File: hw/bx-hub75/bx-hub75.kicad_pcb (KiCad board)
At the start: 2 copper layers, 63.5 x 50.8 mm, 11 parts, among them J1 DB9_Male, U1 74HCT244, U2 74HCT244, U3 LD1117S33TR_SOT223, U4 25LCxxx, U5 SN65HVD77D

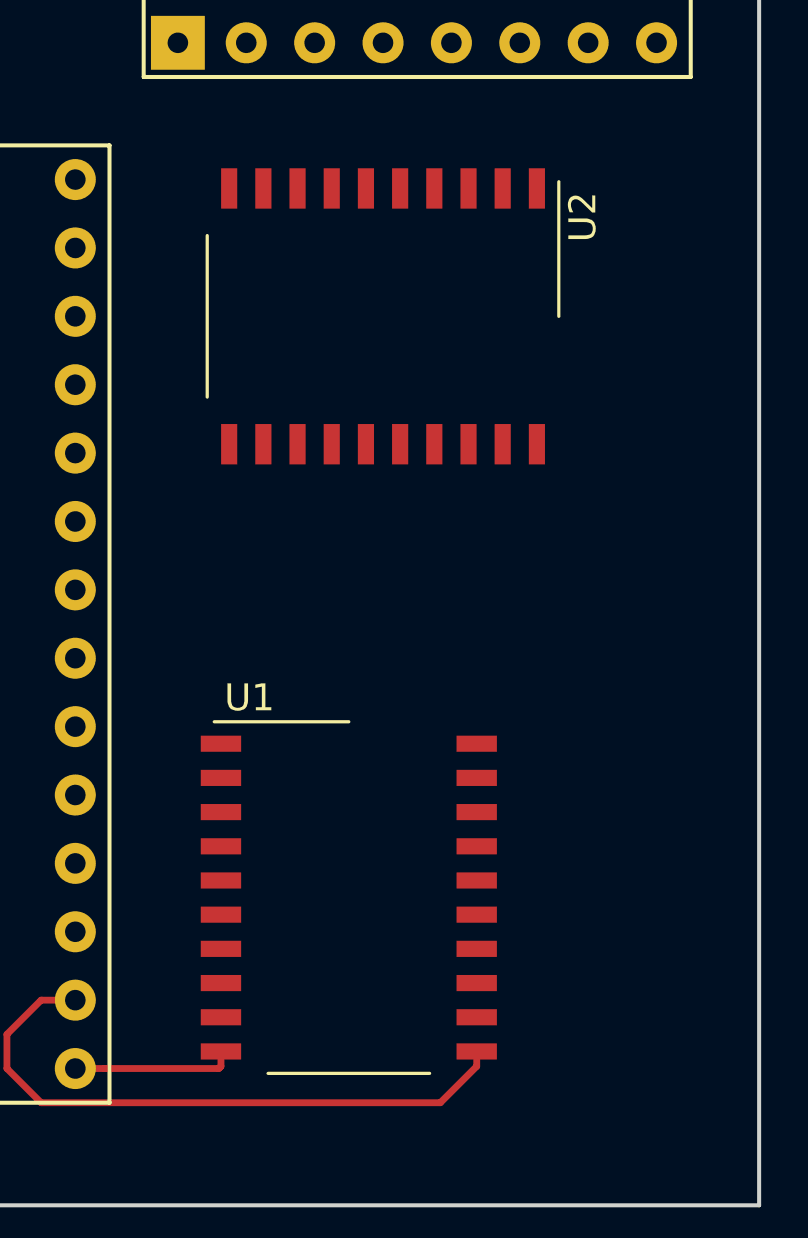
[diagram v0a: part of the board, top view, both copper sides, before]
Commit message: hw/bx-hub75: 74HCT244 -> 74HCT541
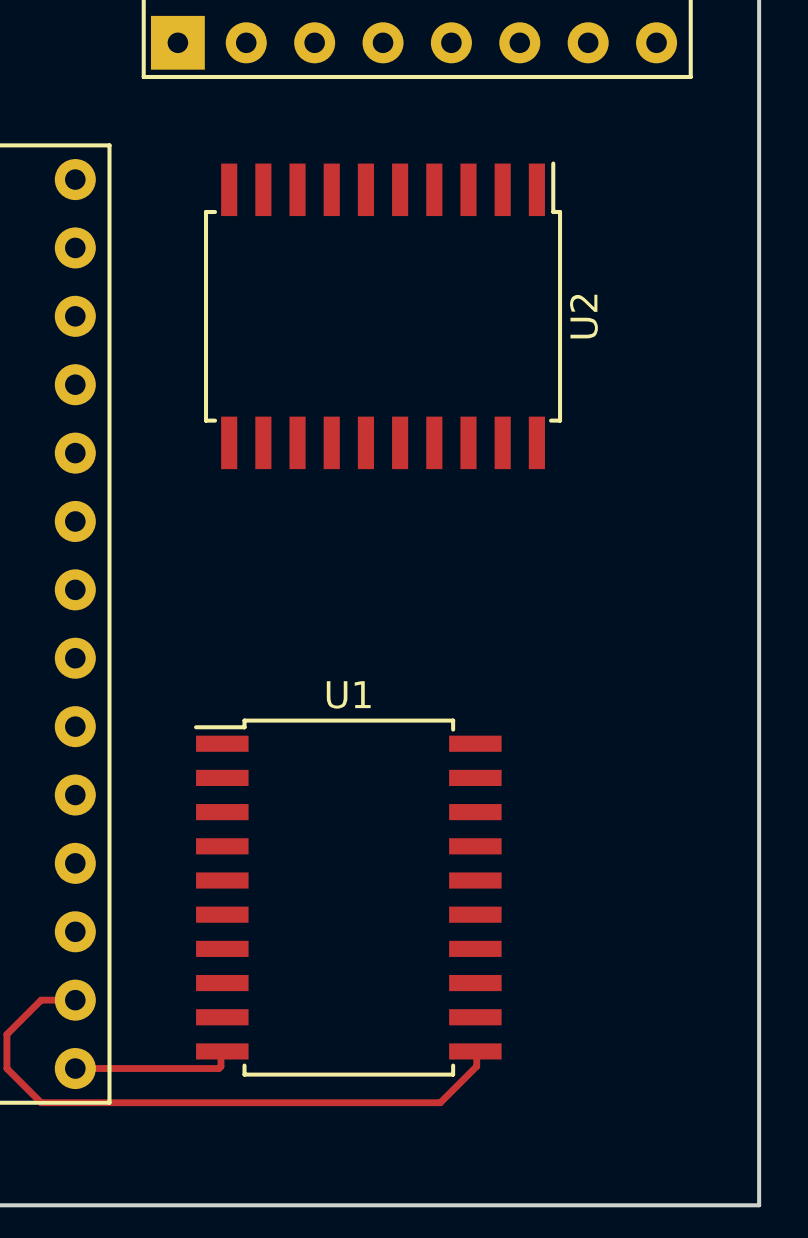
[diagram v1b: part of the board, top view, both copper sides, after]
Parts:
- U1, U2: value 74HCT244 -> 74HCT541; footprint Package_SO:SO-20_12.8x7.5mm_P1.27mm -> Package_SO:SOIC-20W_7.5x12.8mm_P1.27mm
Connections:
- U1 pad 11: /OE -> Net-(CHAIN1-Pad15)
- U1 pad 12: Net-(CHAIN1-Pad7) -> Net-(CHAIN1-Pad13)
- U1 pad 13: /CLK -> Net-(CHAIN1-Pad11)
- U1 pad 14: Net-(CHAIN1-Pad5) -> Net-(CHAIN1-Pad9)
- U1 pad 15: /C -> Net-(CHAIN1-Pad7)
- U1 pad 16: Net-(CHAIN1-Pad3) -> Net-(CHAIN1-Pad5)
- U1 pad 17: /A -> Net-(CHAIN1-Pad3)
- U1 pad 3: Net-(CHAIN1-Pad9) -> /B1
- U1 pad 4: /B1 -> /R2
- U1 pad 5: Net-(CHAIN1-Pad11) -> /B2
- U1 pad 6: /R2 -> /A
- U1 pad 7: Net-(CHAIN1-Pad13) -> /C
- U1 pad 8: /B2 -> /CLK
- U1 pad 9: Net-(CHAIN1-Pad15) -> /OE
- U2 pad 12: Net-(CHAIN1-Pad6) -> Net-(U2-Pad12)
- U2 pad 14: Net-(CHAIN1-Pad10) -> Net-(CHAIN1-Pad2)
- U2 pad 15: Net-(U2-Pad15) -> Net-(CHAIN1-Pad6)
- U2 pad 16: Net-(CHAIN1-Pad12) -> Net-(CHAIN1-Pad10)
- U2 pad 17: /G1 -> Net-(CHAIN1-Pad12)
- U2 pad 3: Net-(CHAIN1-Pad2) -> /D
- U2 pad 4: /D -> /B
- U2 pad 5: Net-(U2-Pad5) -> /G2
- U2 pad 6: /B -> /G1
- U2 pad 8: /G2 -> Net-(U2-Pad8)

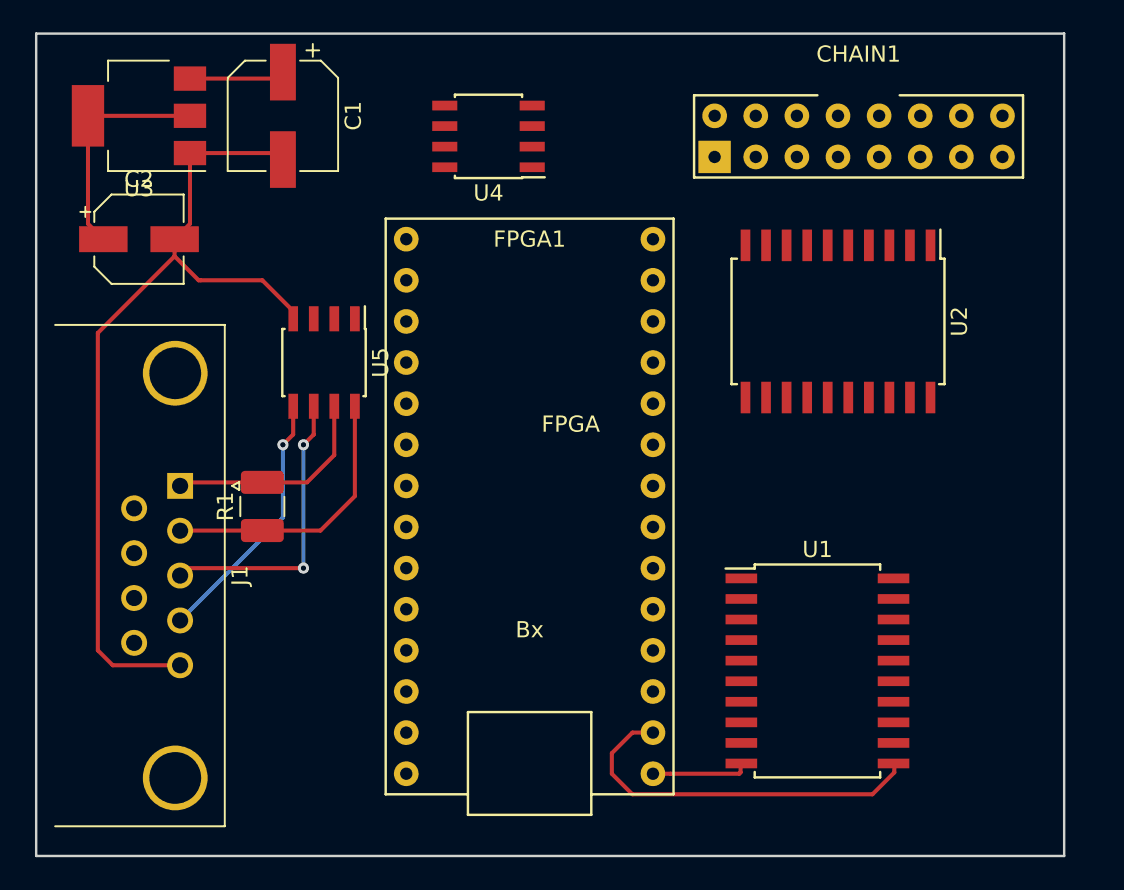
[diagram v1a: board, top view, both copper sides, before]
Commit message: hw/bx-hub75: finish basic routing.
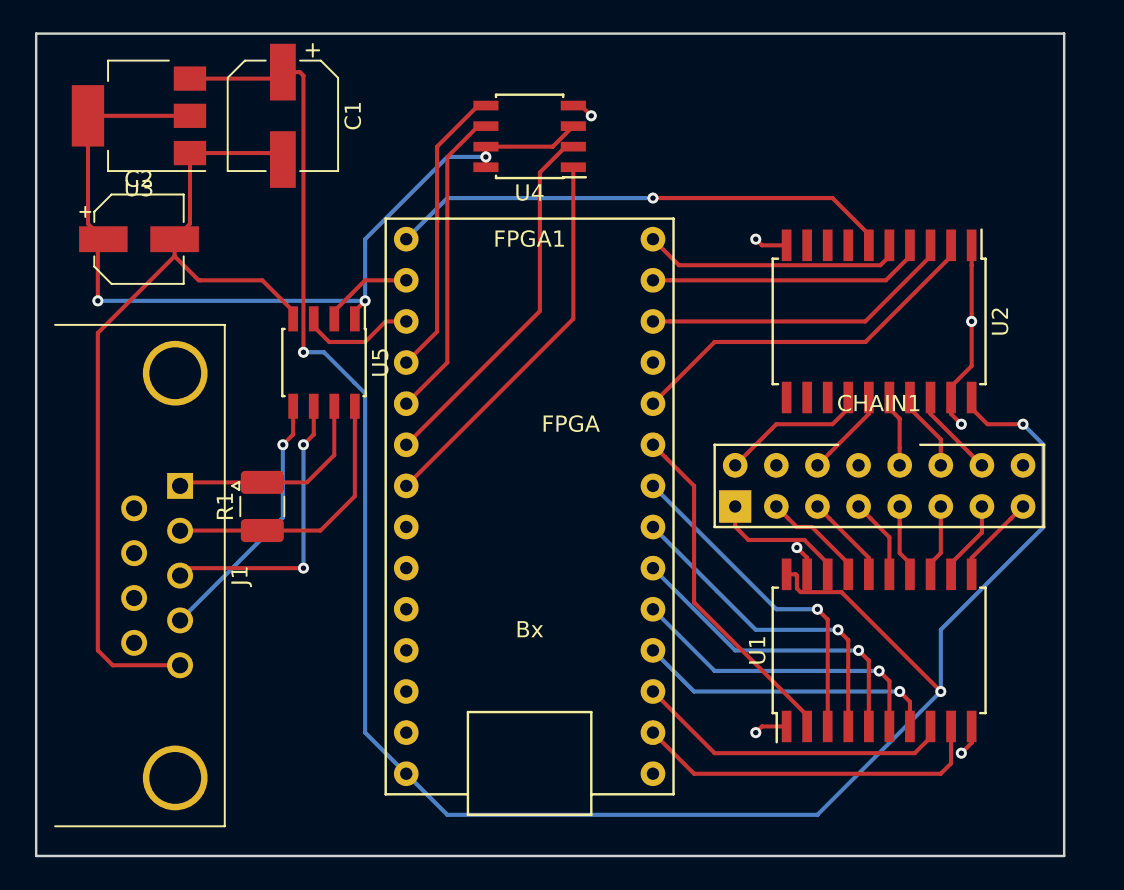
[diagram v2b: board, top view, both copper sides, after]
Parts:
- moved CHAIN1 21.6 mm to (90.2, 91.4)
- moved U1 4.02 mm to (90.2, 101.6), turned to 90 degrees
- moved U2 2.54 mm to (90.2, 81.3)
- moved U4 2.54 mm to (68.6, 69.8)
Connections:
- FPGA1 pad 18: /SCK -> /MOSI
- FPGA1 pad 19: /MISO -> /SCK
- FPGA1 pad 20: /MOSI -> /MISO
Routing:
- net +5V: track 5.91 -> 127.9 mm, vias 0 -> 3
- net +3V3: track 14.3 -> 56.7 mm, vias 0 -> 3
- net /G1: track 0.00 -> 31.2 mm, vias 0 -> 1
- net /CS_EEPROM: track 0.00 -> 24.0 mm
- net /MISO: track 0.00 -> 23.0 mm
- net /LAT: track 0.00 -> 22.9 mm
- net /R1: track 0.00 -> 21.3 mm
- net /B1: track 0.00 -> 20.8 mm, vias 0 -> 1
- net /R2: track 0.00 -> 20.3 mm, vias 0 -> 1
- net /CLK: track 0.00 -> 19.8 mm
- net /B2: track 0.00 -> 19.8 mm, vias 0 -> 1
- net /D: track 0.00 -> 19.5 mm
- net /SCK: track 0.00 -> 19.5 mm
- net /A: track 0.00 -> 19.2 mm, vias 0 -> 1
- net /C: track 0.00 -> 18.7 mm, vias 0 -> 1
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- added copper zone on B.Cu, net GND

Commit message: hw/{library,bx-hub75}: TinyFPGA has 28 pins, not 26...
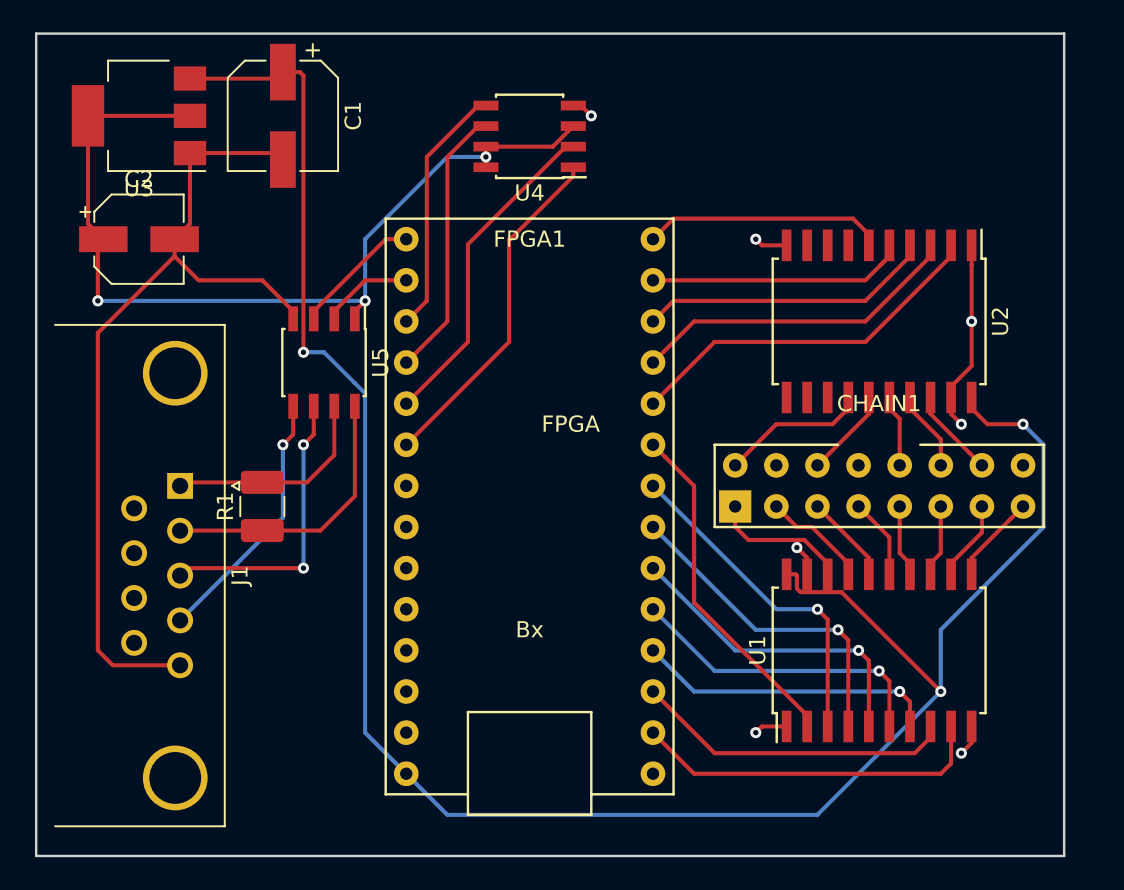
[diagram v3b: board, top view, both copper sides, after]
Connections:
- FPGA1 pad 11: (no net) -> /D
- FPGA1 pad 12: /D -> /B
- FPGA1 pad 13: /B -> /G2
- FPGA1 pad 14: /G2 -> /G1
- FPGA1 pad 15: /G1 -> /TX
- FPGA1 pad 17: /TX -> /MOSI
- FPGA1 pad 18: /MOSI -> /SCK
- FPGA1 pad 19: /SCK -> /MISO
- FPGA1 pad 20: /MISO -> /CS_EEPROM
- FPGA1 pad 21: /CS_EEPROM -> Net-(FPGA1-Pad21)
- FPGA1 pad 25: (no net) -> Net-(FPGA1-Pad25)
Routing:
- net /G1: track 31.2 -> 14.9 mm, vias 1 -> 0
- net /SCK: track 19.5 -> 16.9 mm
- net /MISO: track 23.0 -> 20.4 mm
- net /MOSI: track 18.2 -> 15.7 mm
- net /CS_EEPROM: track 24.0 -> 21.5 mm
- net /B: track 17.2 -> 18.2 mm
- net /D: track 19.5 -> 20.5 mm
- net /TX: track 7.11 -> 8.03 mm
- net /G2: track 16.2 -> 16.7 mm

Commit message: hw/bx-hub75: oshw logo, text, extension header
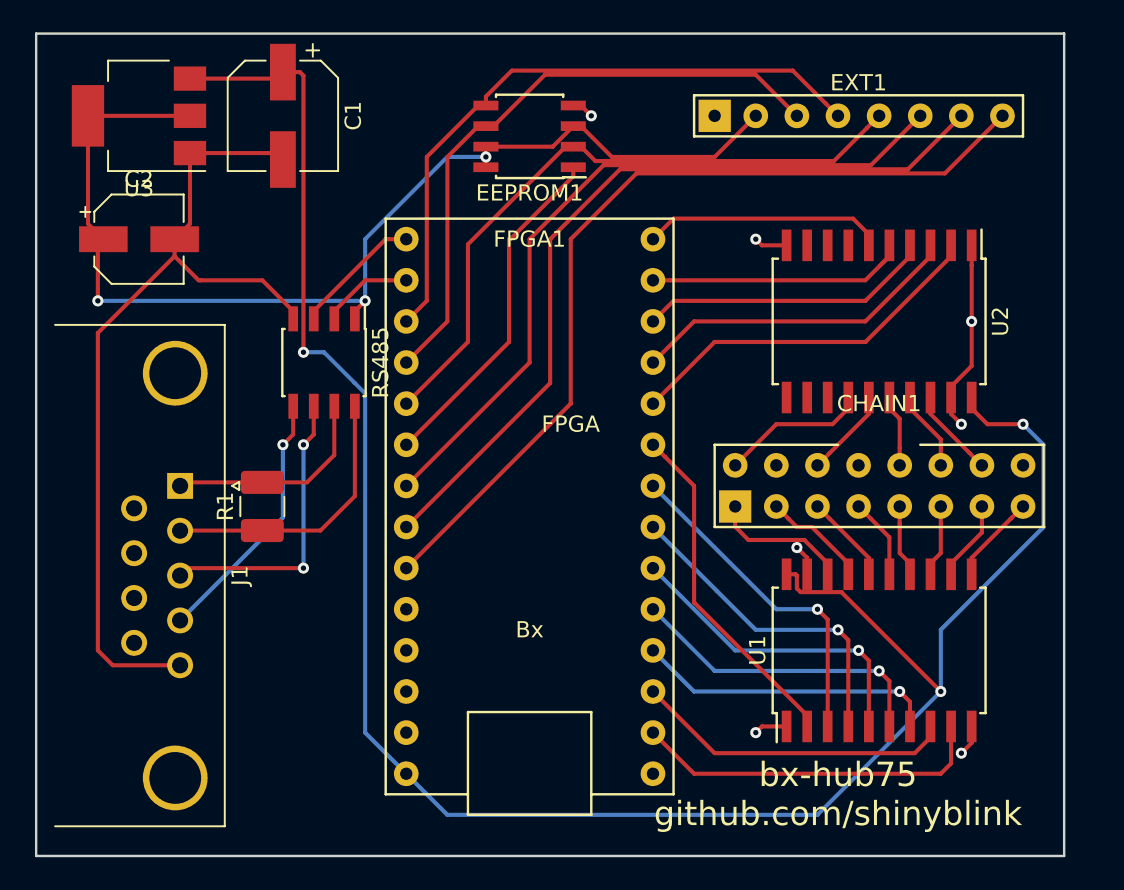
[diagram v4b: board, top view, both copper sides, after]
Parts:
- added EXT1: EXT_HEADER, Random:EXT_HEADER, F.Cu at (88.9, 68.6)
- renumbered U4 to EEPROM1, U5 to RS485
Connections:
- FPGA1 pad 21: Net-(FPGA1-Pad21) -> /SC_EXT
- FPGA1 pad 22: Net-(FPGA1-Pad22) -> /EXT_IO1
- FPGA1 pad 23: Net-(FPGA1-Pad23) -> /EXT_IO2
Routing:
- net /EXT_IO2: track 0.00 -> 54.4 mm
- net /EXT_IO1: track 0.00 -> 50.0 mm
- net /SC_EXT: track 0.00 -> 45.7 mm
- net /MOSI: track 15.7 -> 39.8 mm
- net /SCK: track 16.9 -> 38.5 mm
- net /MISO: track 20.4 -> 40.8 mm
- net +3V3: track 56.7 -> 69.8 mm
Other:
- board text added: "bx-hub75 github.com/shinyblink"

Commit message: hw/bx-hub75: add barrel jack
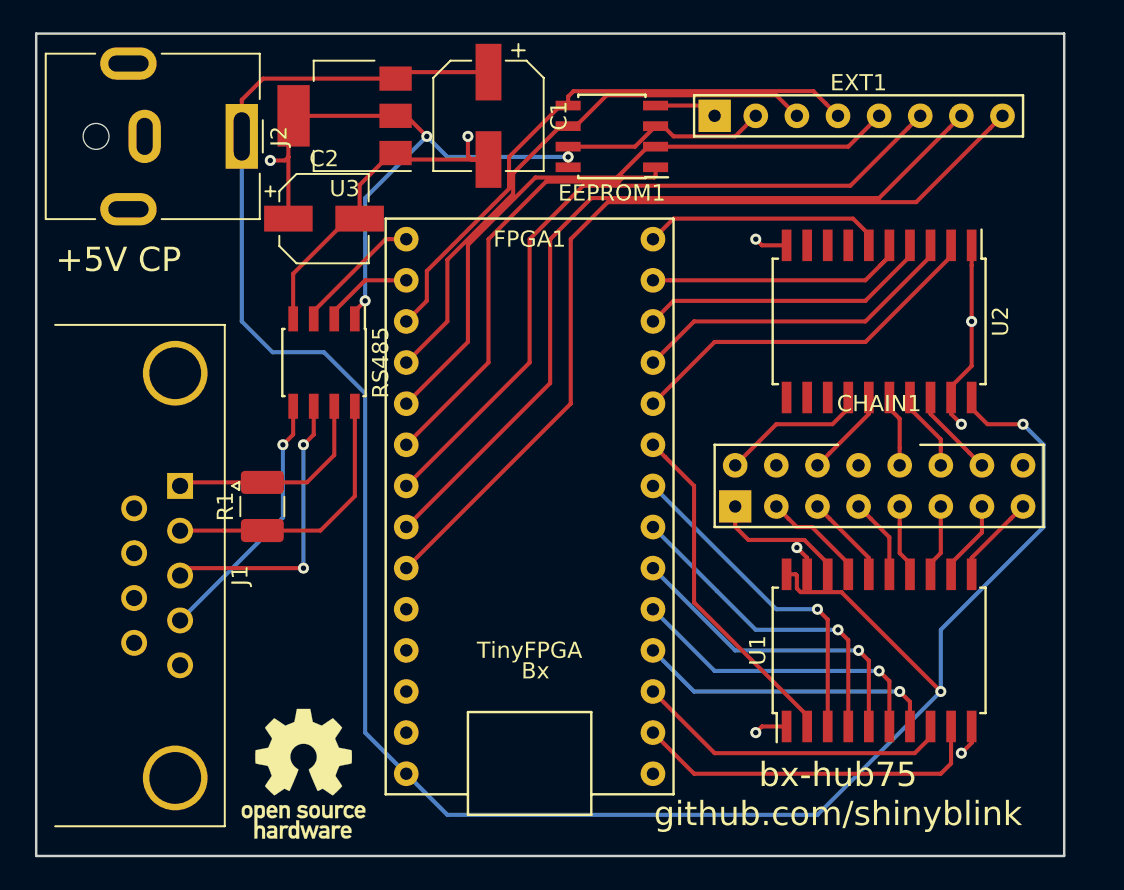
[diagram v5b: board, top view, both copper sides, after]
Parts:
- added J2: Barrel_Jack_MountingPin, Connector_BarrelJack:BarrelJack_CUI_PJ-063AH_Horizontal, F.Cu at (50.8, 69.8)
- added REF**: OSHW-Logo_7.5x8mm_SilkScreen, Symbol:OSHW-Logo_7.5x8mm_SilkScreen, F.Cu at (54.6, 109.2)
- moved C1 12.7 mm to (66.0, 68.6)
- moved U3 12.7 mm to (57.1, 68.6)
- moved C2 11.5 mm to (55.9, 74.9)
- moved EEPROM1 5.08 mm to (73.7, 69.8)
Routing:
- net GND: track 74.8 -> 47.1 mm
- net +3V3: track 69.8 -> 53.0 mm, vias 3 -> 4
- net +5V: track 127.9 -> 138.3 mm, vias 3 -> 2
- net /CS_EEPROM: track 21.5 -> 27.3 mm
- net /MOSI: track 39.8 -> 35.7 mm
- net /SCK: track 38.5 -> 34.5 mm
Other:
- board text added: "+5V CP"

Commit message: hw/bx-hub75: reroute to 0.1m minimum trace spacing
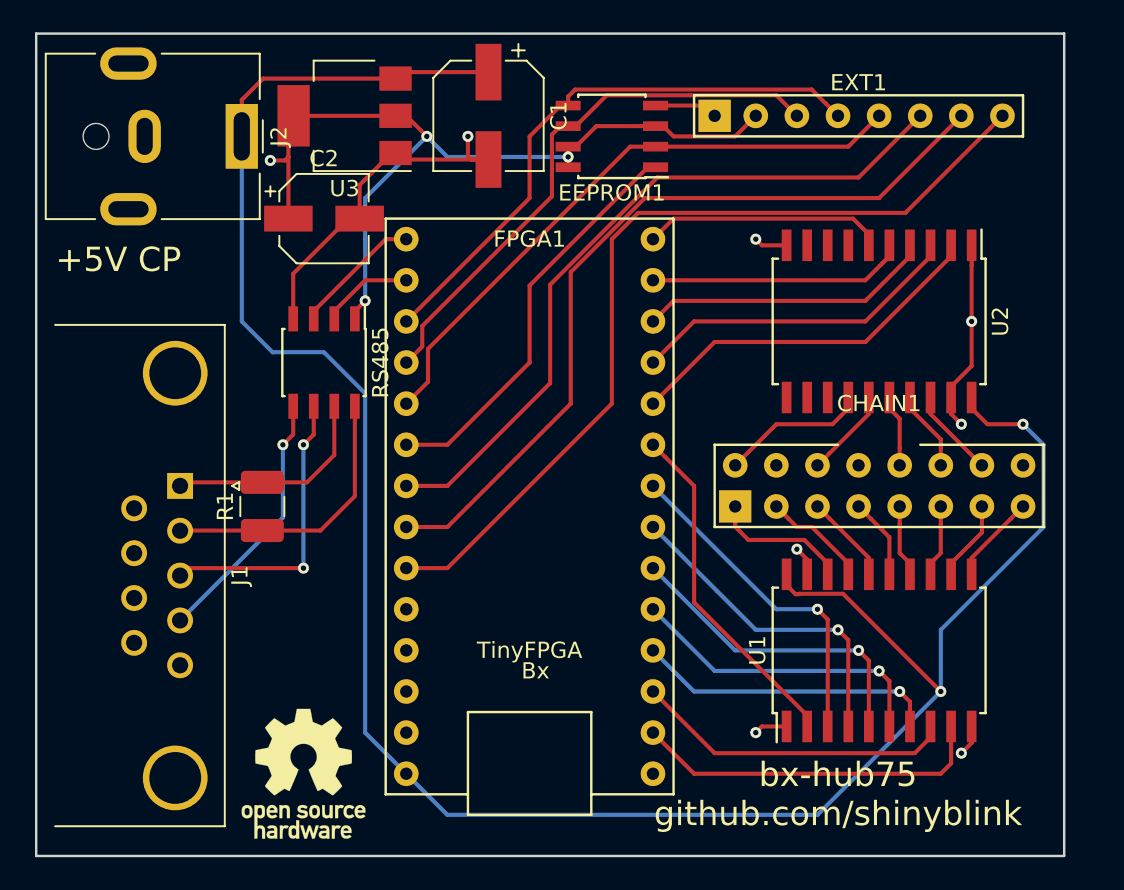
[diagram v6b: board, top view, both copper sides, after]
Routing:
- net /MISO: track 40.6 -> 38.2 mm
- net /CS_EEPROM: track 27.3 -> 25.3 mm
- net /SC_EXT: track 45.7 -> 44.8 mm
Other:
- net class Default: clearance 0 -> 0.1
- rule trace_clearance: 0 -> 0.1

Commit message: hw/bx-hub75: allow bom generation with kibom
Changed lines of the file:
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@@
   (module Random:HUB75_HEADER (layer F.Cu)
     (at 90.17 91.44 180)
-    (fp_text reference CHAIN1 (at 0 5.08 180) (layer F.SilkS)
+    (fp_text reference CHAIN1 (at 11.43 0 270) (layer F.SilkS)
       (effects (font (size 1 1) (thickness 0.15)))
     )
-    (fp_text value HUB75_HEADER (at 0 -4.31 180) (layer F.Fab)
+    (fp_text value HUB75_HEADER (at 0 0 180) (layer F.Fab)
       (effects (font (size 1 1) (thickness 0.15)))
     )

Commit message: hw/bx-hub75: V0.2 PCB/SCH.
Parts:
- removed the REF** at (54.6, 109.2)
- added JP1: EXTPWR, Connector_PinHeader_2.54mm:PinHeader_1x02_P2.54mm_Vertical, F.Cu at (45.7, 78.7)
- added R2: 120, Resistor_SMD:R_1210_3225Metric_Pad1.42x2.65mm_HandSolder, F.Cu at (52.1, 99.1)
- added REF**: OSHW-Logo2_9.8x8mm_SilkScreen, Symbol:OSHW-Logo2_9.8x8mm_SilkScreen, F.Cu at (55.9, 109.2)
- EXT1: footprint Random:EXT_HEADER -> Connector_PinHeader_2.54mm:PinHeader_1x08_P2.54mm_Vertical
- moved EXT1 8.89 mm to (80.0, 68.6), turned to 90 degrees
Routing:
- net Net-(J1-Pad6): track 0.00 -> 15.5 mm
- net /TX-: track 16.1 -> 21.5 mm
- net +5V: track 138.3 -> 140.4 mm
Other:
- board text added: "+5V"
- board text added: "bx-hub75 V0.2 github.com/shinyblink"
- board text removed: "+5V CP"
- board text removed: "bx-hub75 github.com/shinyblink"
